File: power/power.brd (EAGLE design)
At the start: 40.3 x 38.1 mm, 8 parts, among them IC1 LD117AS33TR, J1 ESP-STACK-HEADER

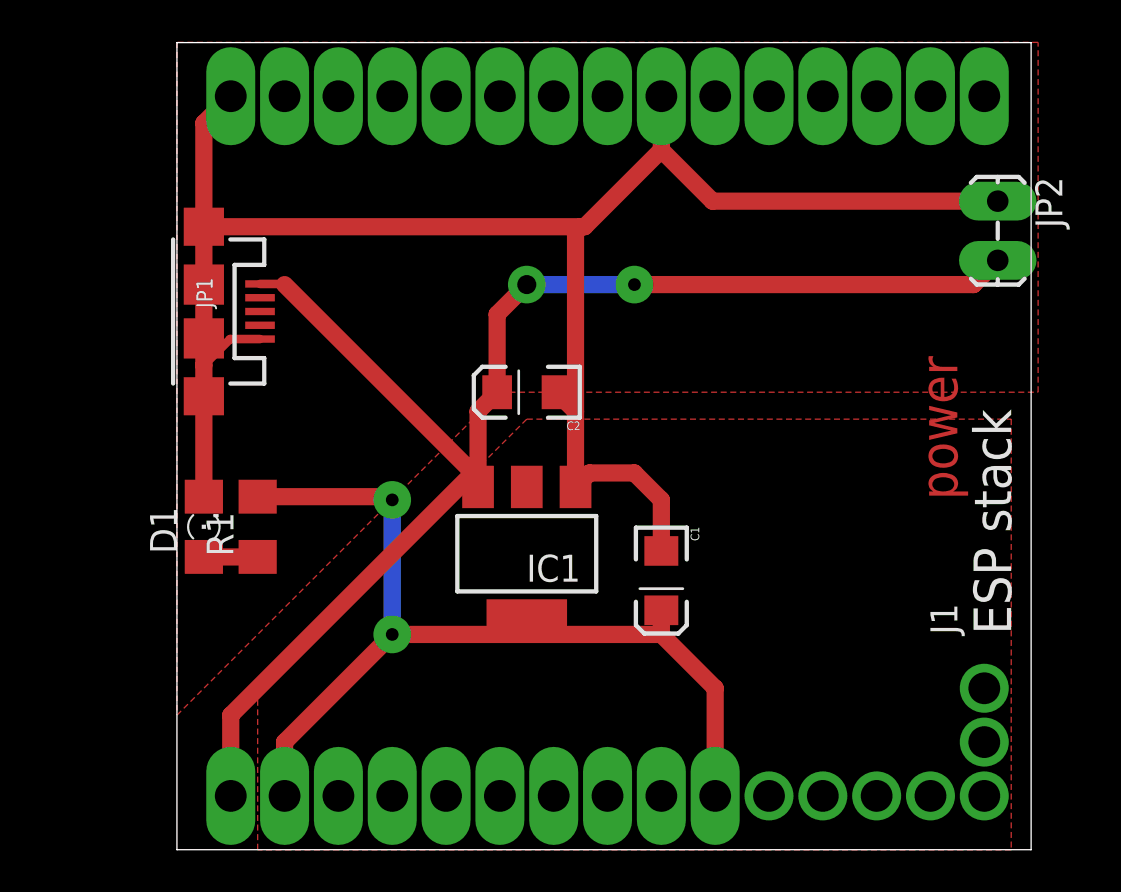
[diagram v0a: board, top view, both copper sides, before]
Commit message: Power/FTDI board
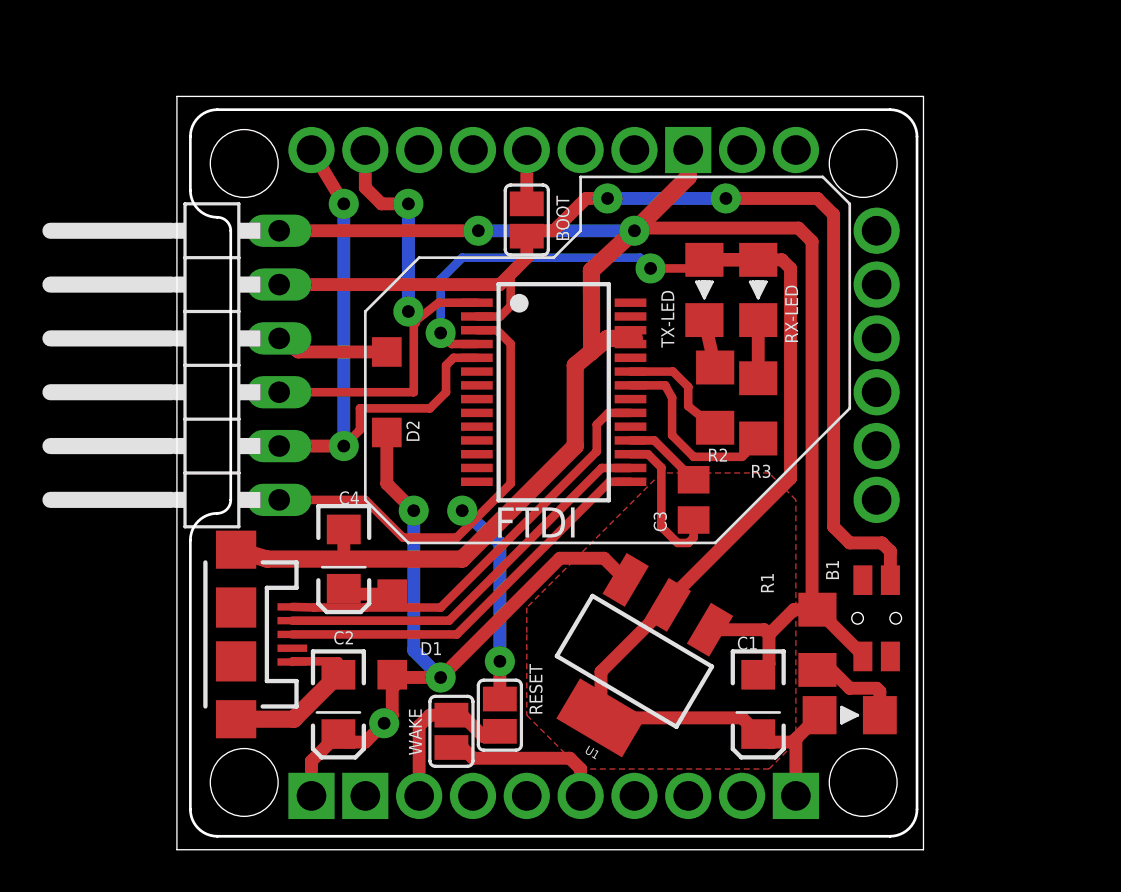
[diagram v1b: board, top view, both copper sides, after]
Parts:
- removed IC1: LD117AS33TR, v-reg:SOT223
- removed J1: ESP-STACK-HEADER, ESPstack:ESP-STACK-HEADER
- removed JP2: (no value), SparkFun-Connectors:1X02_LOCK_LONGPADS
- added B1: (no value), ESPstack:SKSCLDE010
- added BOOT, RESET, WAKE: (no value), jumper:SJ
- added C3: 100nF, eagle-ltspice:C0805
- added C4: 10uF, SparkFun-Capacitors:EIA3216
- added D2: MBR120, ESPstack:SOD123
- added H1: ESP-BOARD, ESPstack:ESP-BOARD
- added IC2: FT232RL, ftdichip:SSOP28
- added JP3: (no value), pinhead:1X06/90
- added POWER, RX-LED, TX-LED: DIODE_SMDD1206, diodes_gen:D1206
- added R2, R3: 1k, dp_devices:R1206
- added U1: (no value), SparkFun-PowerIC:SOT223
- D1: value (none) -> MBR120; device SparkFun-LED:FKIT-LED-1206 -> ESPstack:SOD123
- moved R1 26.9 mm to (30.2, 9.91), turned to 270 degrees
- moved C2 17.2 mm to (7.62, 6.86), turned to 270 degrees
- moved JP1 15.3 mm to (2.79, 10.2)
- moved D1 10.2 mm to (10.2, 10.2)
- moved C1 7.42 mm to (27.4, 6.86)
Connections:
- new net +5V: C4.A, D1.A, IC2.20, JP1.VBUS
- new net D+: IC2.15, JP1.D+
- new net D-: IC2.16, JP1.D-
- new net DTR: B1.1, B1.2, BOOT.2, IC2.2, JP3.5
- new net GPIO0: BOOT.1, H1.GPIO0
- new net GPIO16: H1.GPIO16, WAKE.1
- new net N$16: C3.1, IC2.17
- new net N$2: IC2.22, R3.1
- new net N$3: R2.2, TX-LED.K
- new net N$4: IC2.23, R2.1
- new net N$8: D2.A, JP3.4
- new net N$9: R3.2, RX-LED.K
- new net RST: H1.RST, RESET.2, WAKE.2
- new net RTS: IC2.3, JP3.1, RESET.1
- new net RXD: H1.TXD0, IC2.5, JP3.2
- new net TXD: H1.RXD0, IC2.1, JP3.3
- new net VBATT: H1.VBATT
- net +3V3: now also H1.VCC, IC2.4, POWER.A, RX-LED.A, TX-LED.A, U1.2, U1.4; no longer IC1.4, J1.3V3@1, J1.3V3@2, R1.2
- net GND: now also B1.3, B1.4, C3.2, C4.C, H1.GND, IC2.18, IC2.21, IC2.25, IC2.26, IC2.7, JP3.6, R1.1, U1.1; no longer D1.C, IC1.1, J1.GND@1, J1.GND@2, JP2.1
- net N$1: now also POWER.K, R1.2; no longer D1.A, R1.1
- net V+: now also D1.C, D2.C, H1.V+, U1.3; no longer IC1.3, J1.VBAT, JP1.VBUS, JP2.2
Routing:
- net DTR: track 0.00 -> 51.7 mm, vias 0 -> 2
- net V+: track 67.7 -> 35.2 mm, vias 2 -> 3
- net RTS: track 0.00 -> 31.6 mm, vias 0 -> 2
- net RXD: track 0.00 -> 26.8 mm, vias 0 -> 2
- net +5V: track 0.00 -> 24.5 mm
- net TXD: track 0.00 -> 22.8 mm, vias 0 -> 2
- net D-: track 0.00 -> 18.9 mm
- net D+: track 0.00 -> 18.9 mm
- net GND: track 86.0 -> 104.1 mm, vias 0 -> 2
- net +3V3: track 45.9 -> 63.7 mm
- net N$2: track 0.00 -> 8.98 mm
- net RST: track 0.00 -> 7.85 mm
- net GPIO16: track 0.00 -> 7.79 mm
- net N$16: track 0.00 -> 7.28 mm
- net N$4: track 0.00 -> 5.56 mm
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- removed copper zone on layer 1, net GND
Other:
- board size 40.3 x 38.1 mm -> 35.2 x 35.5 mm
- board text added: "FTDI"
- board text removed: "power"

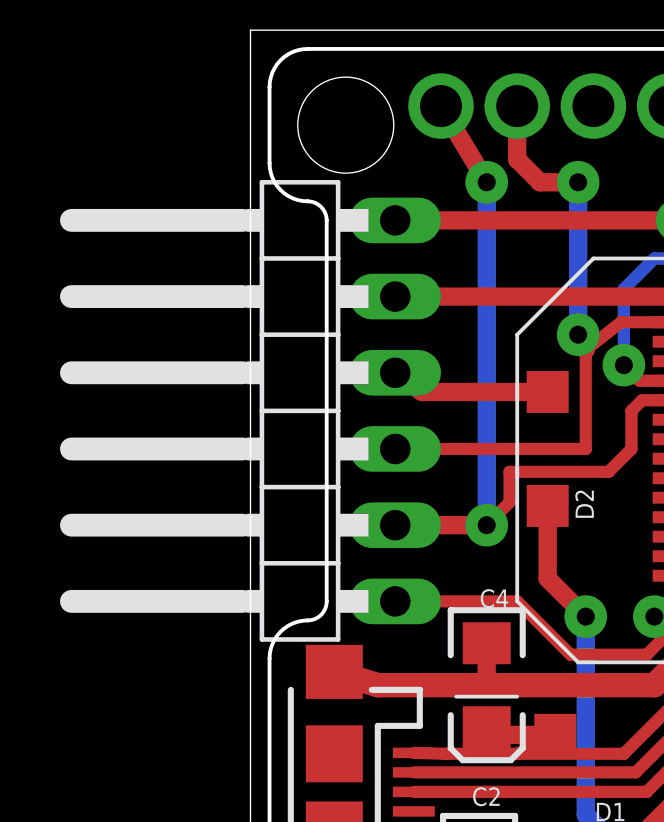
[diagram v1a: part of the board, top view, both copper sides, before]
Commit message: Power board (USB, external power, FT232RL section
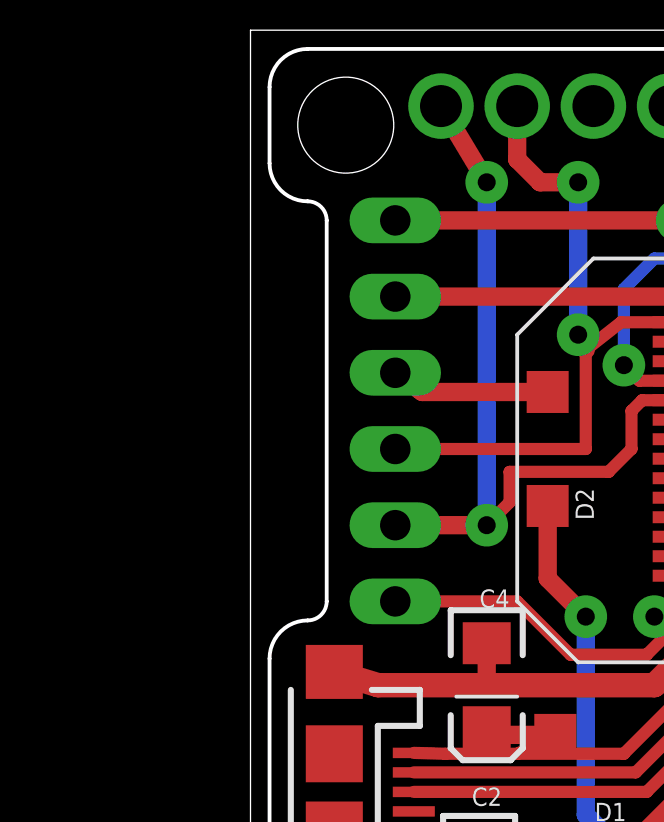
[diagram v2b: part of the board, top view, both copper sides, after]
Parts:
- JP3: device pinhead:1X06/90 -> ESPstack:1X06
- moved JP3 3.81 mm to (4.83, 22.9)
- renumbered H1 to POWER/FTDI
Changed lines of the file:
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@@
 <attribute name="NAME" x="27.559" y="13.081" size="0.6096" layer="25" font="vector" ratio="10" rot="R270"/>
 </element>
-<element name="H1" library="ESPstack" package="ESP-BOARD" value="ESP-BOARD" x="24.13" y="19.05"/>
+<element name="POWER/FTDI" library="ESPstack" package="ESP-BOARD" value="ESP-BOARD" x="24.13" y="19.05"/>
 <element name="IC2" library="ftdichip" package="SSOP28" value="FT232RL" x="17.78" y="21.59" smashed="yes" rot="R270">
 <attribute name="OC_FARNELL" value="1146032" x="17.78" y="21.59" size="1.778" layer="27" rot="R270" display="off"/>
@@
 <attribute name="VALUE" x="15.24" y="5.9499" size="0.02" layer="27" rot="R270"/>
 </element>
-<element name="JP3" library="pinhead" package="1X06/90" value="" x="1.016" y="22.86" smashed="yes" rot="R90">
-<attribute name="VALUE" x="4.191" y="15.24" size="1.27" layer="27" rot="R90"/>
+<element name="JP3" library="ESPstack" package="1X06" value="" x="4.826" y="22.86" smashed="yes" rot="R90">
+<attribute name="VALUE" x="8.001" y="15.24" size="1.27" layer="27" rot="R90"/>
 </element>
 <element name="C4" library="SparkFun-Capacitors" package="EIA3216" value="10uF" x="7.874" y="13.716" smashed="yes" rot="R270">
@@
 <signal name="V+">
 <contactref element="C2" pad="A"/>
-<contactref element="H1" pad="V+"/>
+<contactref element="POWER/FTDI" pad="V+"/>
 <contactref element="D1" pad="C"/>
 <contactref element="D2" pad="C"/>
@@
 </signal>
 <signal name="+3V3">
-<contactref element="H1" pad="VCC"/>
+<contactref element="POWER/FTDI" pad="VCC"/>
 <contactref element="C1" pad="A"/>
 <contactref element="IC2" pad="4"/>
@@
 <contactref element="C1" pad="C"/>
 <contactref element="C2" pad="C"/>
-<contactref element="H1" pad="GND"/>
+<contactref element="POWER/FTDI" pad="GND"/>
 <contactref element="IC2" pad="7"/>
 <contactref element="IC2" pad="18"/>
@@
 </signal>
 <signal name="VBATT">
-<contactref element="H1" pad="VBATT"/>
+<contactref element="POWER/FTDI" pad="VBATT"/>
 </signal>
 <signal name="DTR">
@@
 </signal>
 <signal name="GPIO0">
-<contactref element="H1" pad="GPIO0"/>
+<contactref element="POWER/FTDI" pad="GPIO0"/>
 <contactref element="BOOT" pad="1"/>
 <wire x1="17.272" y1="32.258" x2="16.51" y2="33.02" width="0" layer="19" extent="1-16"/>
@@
 <signal name="RST">
 <contactref element="WAKE" pad="2"/>
-<contactref element="H1" pad="RST"/>
+<contactref element="POWER/FTDI" pad="RST"/>
 <contactref element="RESET" pad="2"/>
 <wire x1="12.954" y1="6.35" x2="11.938" y2="6.35" width="0.6096" layer="1"/>
@@
 <signal name="TXD">
 <contactref element="IC2" pad="1"/>
-<contactref element="H1" pad="RXD0"/>
+<contactref element="POWER/FTDI" pad="RXD0"/>
 <contactref element="JP3" pad="3"/>
 <wire x1="4.826" y1="21.59" x2="11.176" y2="21.59" width="0.4064" layer="1"/>
@@
 <signal name="RXD">
 <contactref element="IC2" pad="5"/>
-<contactref element="H1" pad="TXD0"/>
+<contactref element="POWER/FTDI" pad="TXD0"/>
 <contactref element="JP3" pad="2"/>
 <wire x1="14.155" y1="23.215" x2="13.055" y2="23.215" width="0.4064" layer="1"/>
@@
 <signal name="GPIO16">
 <contactref element="WAKE" pad="1"/>
-<contactref element="H1" pad="GPIO16"/>
+<contactref element="POWER/FTDI" pad="GPIO16"/>
 <wire x1="12.954" y1="4.826" x2="13.462" y2="4.826" width="0.6096" layer="1"/>
 <wire x1="13.462" y1="4.826" x2="13.97" y2="4.318" width="0.6096" layer="1"/>

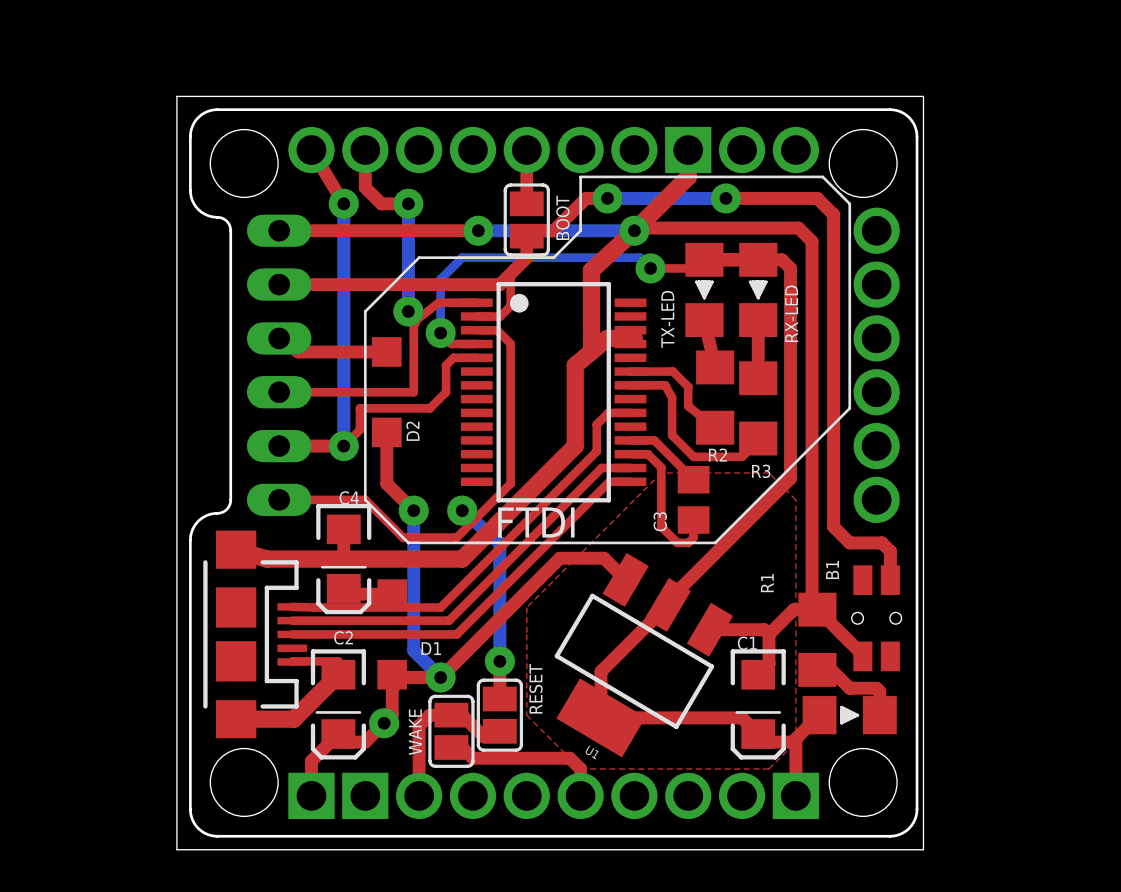
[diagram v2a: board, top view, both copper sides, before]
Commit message: Small improvements to usb board
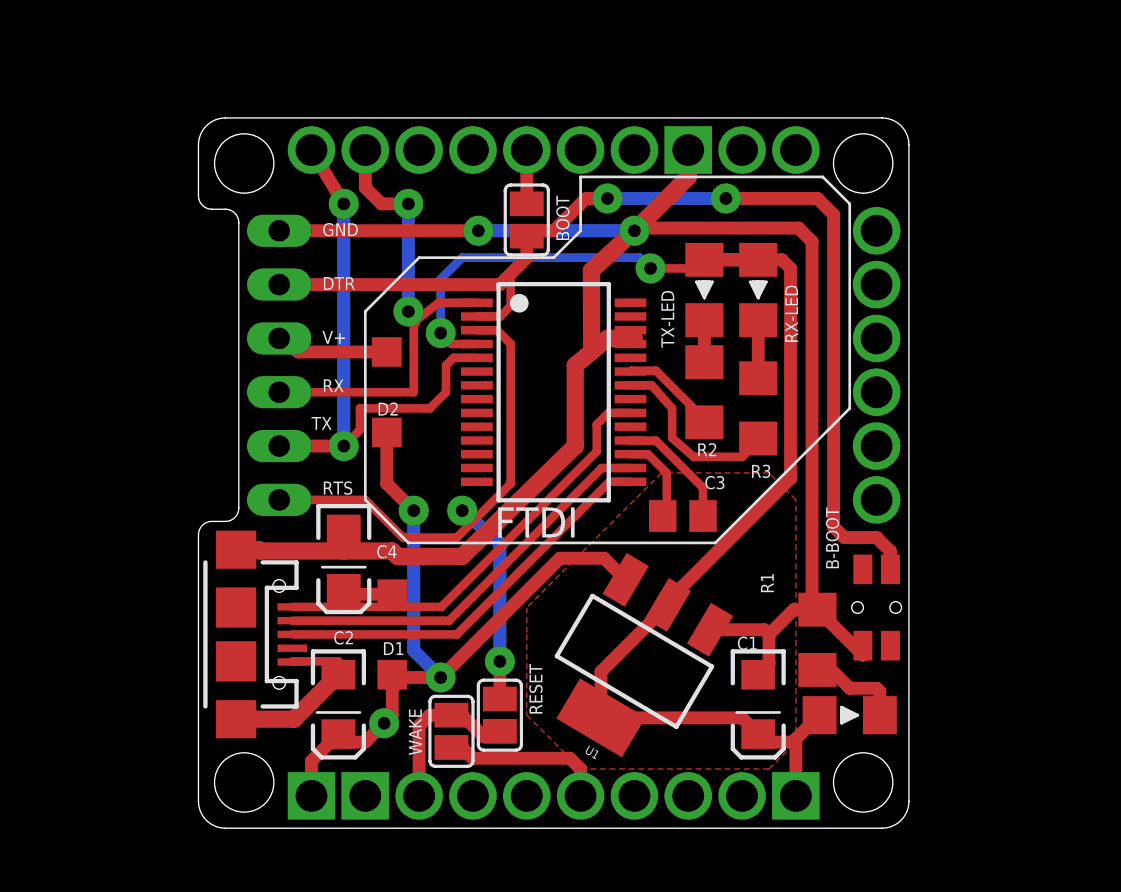
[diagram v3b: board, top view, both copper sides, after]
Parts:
- removed B1: (no value), ESPstack:SKSCLDE010
- added B-BOOT: (no value), ESPstack:SKSCLDE010
- moved C3 0.92 mm to (23.9, 15.7), turned to 0 degrees
- moved R2 0.57 mm to (24.9, 21.6)
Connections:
- net DTR: now also B-BOOT.1, B-BOOT.2; no longer B1.1, B1.2
- net GND: now also B-BOOT.3, B-BOOT.4; no longer B1.3, B1.4
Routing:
- net N$16: track 7.28 -> 4.19 mm
- net GND: track 104.1 -> 106.0 mm
- net N$4: track 5.56 -> 4.60 mm
- net +5V: track 24.5 -> 23.6 mm
- net DTR: track 51.7 -> 51.2 mm
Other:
- board size 35.2 x 35.5 mm -> 33.5 x 33.5 mm
- board text added: "DTR"
- board text added: "GND"
- board text added: "RTS"
- board text added: "RX"
- board text added: "TX"
- board text added: "V+"
